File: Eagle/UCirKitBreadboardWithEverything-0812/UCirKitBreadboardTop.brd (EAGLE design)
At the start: 64.8 x 100 mm, 600 parts

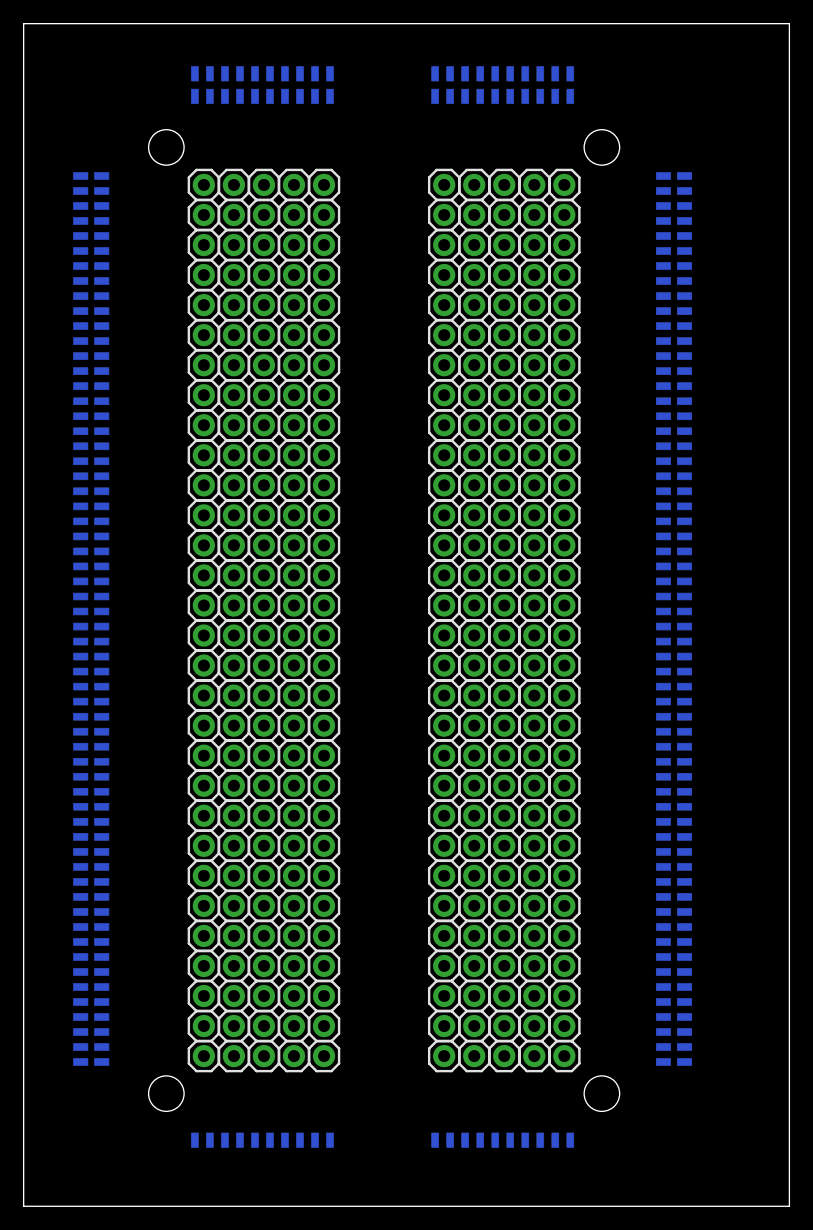
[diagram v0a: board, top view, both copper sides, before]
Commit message: UCirKitBreadboardTop completes routing!
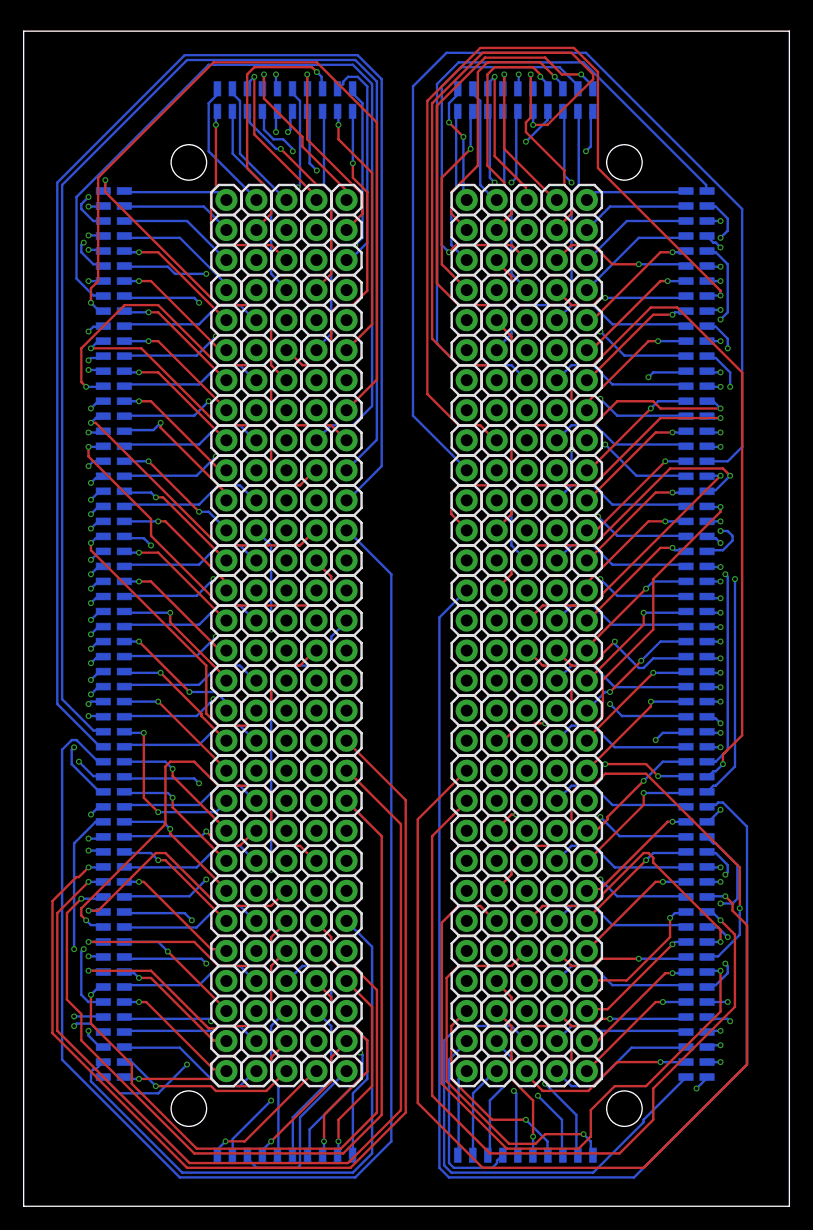
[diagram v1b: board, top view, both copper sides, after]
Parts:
- moved JP1022 2.29 mm to (56.0, 84.6)
- moved JP1026 2.29 mm to (56.0, 79.5)
- moved JP1029 2.29 mm to (56.0, 75.7)
- moved JP1033 2.29 mm to (56.0, 70.6)
- moved JP1037 2.29 mm to (56.0, 65.5)
- moved JP63 2.29 mm to (22.2, 69.8)
- moved JP64 2.29 mm to (24.8, 69.8)
- moved JP65 2.29 mm to (27.3, 69.8)
- moved JP66 2.29 mm to (37.5, 69.8)
- moved JP67 2.29 mm to (40.0, 69.8)
- moved JP68 2.29 mm to (42.5, 69.8)
- moved JP69 2.29 mm to (45.1, 69.8)
- moved JP70 2.29 mm to (47.6, 69.8)
- moved JP83 2.29 mm to (22.2, 64.8)
- moved JP84 2.29 mm to (24.8, 64.8)
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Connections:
- net 0_1439380519 renamed 0_1439385713
- net 0_1439380547 renamed 0_1439385741
- net 0_1439380570 renamed 0_1439385798
- net 0_1439380605 renamed 0_1439385823
- net 0_1439380652 renamed 0_1439385772
- net 0_1439380747 renamed 0_1439385849
- net 10_1439380519 renamed 10_1439385713
- net 10_1439380547 renamed 10_1439385741
- net 10_1439380570 renamed 10_1439385798
- net 10_1439380605 renamed 10_1439385823
- net 10_1439380652 renamed 10_1439385772
- net 10_1439380747 renamed 10_1439385849
- net 11_1439380519 renamed 11_1439385713
- net 11_1439380547 renamed 11_1439385741
- net 11_1439380570 renamed 11_1439385798
- net 11_1439380605 renamed 11_1439385823
- net 11_1439380652 renamed 11_1439385772
- net 11_1439380747 renamed 11_1439385849
- net 12_1439380519 renamed 12_1439385713
- net 12_1439380547 renamed 12_1439385741
- net 12_1439380570 renamed 12_1439385798
- net 12_1439380605 renamed 12_1439385823
- net 12_1439380652 renamed 12_1439385772
- net 12_1439380747 renamed 12_1439385849
- net 13_1439380519 renamed 13_1439385713
- net 13_1439380547 renamed 13_1439385741
- net 13_1439380570 renamed 13_1439385798
- net 13_1439380605 renamed 13_1439385823
- net 13_1439380652 renamed 13_1439385772
- net 13_1439380747 renamed 13_1439385849
- net 14_1439380519 renamed 14_1439385713
- net 14_1439380547 renamed 14_1439385741
- net 14_1439380570 renamed 14_1439385798
- net 14_1439380605 renamed 14_1439385823
- net 14_1439380652 renamed 14_1439385772
- net 14_1439380747 renamed 14_1439385849
- net 15_1439380519 renamed 15_1439385713
- net 15_1439380547 renamed 15_1439385741
- net 15_1439380570 renamed 15_1439385798
- net 15_1439380605 renamed 15_1439385823
- net 15_1439380652 renamed 15_1439385772
- net 15_1439380747 renamed 15_1439385849
- net 16_1439380519 renamed 16_1439385713
- net 16_1439380547 renamed 16_1439385741
- net 16_1439380570 renamed 16_1439385798
- net 16_1439380605 renamed 16_1439385823
- net 16_1439380652 renamed 16_1439385772
- net 16_1439380747 renamed 16_1439385849
- net 17_1439380519 renamed 17_1439385713
- net 17_1439380547 renamed 17_1439385741
- net 17_1439380570 renamed 17_1439385798
- net 17_1439380605 renamed 17_1439385823
- net 17_1439380652 renamed 17_1439385772
- net 17_1439380747 renamed 17_1439385849
- net 18_1439380519 renamed 18_1439385713
- net 18_1439380547 renamed 18_1439385741
- net 18_1439380570 renamed 18_1439385798
- net 18_1439380605 renamed 18_1439385823
- net 18_1439380652 renamed 18_1439385772
- net 18_1439380747 renamed 18_1439385849
- net 19_1439380519 renamed 19_1439385713
- net 19_1439380547 renamed 19_1439385741
- net 19_1439380570 renamed 19_1439385798
- net 19_1439380605 renamed 19_1439385823
- net 19_1439380652 renamed 19_1439385772
- net 19_1439380747 renamed 19_1439385849
- net 1_1439380519 renamed 1_1439385713
- net 1_1439380547 renamed 1_1439385741
- net 1_1439380570 renamed 1_1439385798
- net 1_1439380605 renamed 1_1439385823
- net 1_1439380652 renamed 1_1439385772
- net 1_1439380747 renamed 1_1439385849
- net 20_1439380519 renamed 20_1439385713
- net 20_1439380547 renamed 20_1439385741
- net 20_1439380570 renamed 20_1439385798
- net 20_1439380605 renamed 20_1439385823
- net 20_1439380652 renamed 20_1439385772
- net 20_1439380747 renamed 20_1439385849
- net 21_1439380519 renamed 21_1439385713
- net 21_1439380547 renamed 21_1439385741
- net 21_1439380570 renamed 21_1439385798
- net 21_1439380605 renamed 21_1439385823
- net 21_1439380652 renamed 21_1439385772
- net 21_1439380747 renamed 21_1439385849
- net 22_1439380519 renamed 22_1439385713
- net 22_1439380547 renamed 22_1439385741
- net 22_1439380570 renamed 22_1439385798
- net 22_1439380605 renamed 22_1439385823
- net 22_1439380652 renamed 22_1439385772
- net 22_1439380747 renamed 22_1439385849
- net 23_1439380519 renamed 23_1439385713
- net 23_1439380547 renamed 23_1439385741
- net 23_1439380570 renamed 23_1439385798
- net 23_1439380605 renamed 23_1439385823
- net 23_1439380652 renamed 23_1439385772
- net 23_1439380747 renamed 23_1439385849
- net 24_1439380519 renamed 24_1439385713
- net 24_1439380547 renamed 24_1439385741
- net 24_1439380570 renamed 24_1439385798
- net 24_1439380605 renamed 24_1439385823
- net 24_1439380652 renamed 24_1439385772
- net 24_1439380747 renamed 24_1439385849
- net 25_1439380519 renamed 25_1439385713
- net 25_1439380547 renamed 25_1439385741
- net 25_1439380570 renamed 25_1439385798
- net 25_1439380605 renamed 25_1439385823
- net 25_1439380652 renamed 25_1439385772
- net 25_1439380747 renamed 25_1439385849
- net 26_1439380519 renamed 26_1439385713
- net 26_1439380547 renamed 26_1439385741
- net 26_1439380570 renamed 26_1439385798
- net 26_1439380605 renamed 26_1439385823
- net 26_1439380652 renamed 26_1439385772
- net 26_1439380747 renamed 26_1439385849
- net 27_1439380519 renamed 27_1439385713
- net 27_1439380547 renamed 27_1439385741
- net 27_1439380570 renamed 27_1439385798
- net 27_1439380605 renamed 27_1439385823
- net 27_1439380652 renamed 27_1439385772
- net 27_1439380747 renamed 27_1439385849
- net 28_1439380519 renamed 28_1439385713
- net 28_1439380547 renamed 28_1439385741
- net 28_1439380570 renamed 28_1439385798
- net 28_1439380605 renamed 28_1439385823
- net 28_1439380652 renamed 28_1439385772
- net 28_1439380747 renamed 28_1439385849
- net 29_1439380519 renamed 29_1439385713
- net 29_1439380547 renamed 29_1439385741
- net 29_1439380570 renamed 29_1439385798
- net 29_1439380605 renamed 29_1439385823
- net 29_1439380652 renamed 29_1439385772
- net 29_1439380747 renamed 29_1439385849
- net 2_1439380519 renamed 2_1439385713
- net 2_1439380547 renamed 2_1439385741
- net 2_1439380570 renamed 2_1439385798
- net 2_1439380605 renamed 2_1439385823
- net 2_1439380652 renamed 2_1439385772
- net 2_1439380747 renamed 2_1439385849
- net 30_1439380519 renamed 30_1439385713
- net 30_1439380570 renamed 30_1439385798
- net 30_1439380652 renamed 30_1439385772
- net 30_1439380747 renamed 30_1439385849
- net 31_1439380519 renamed 31_1439385713
- net 31_1439380570 renamed 31_1439385798
- net 31_1439380652 renamed 31_1439385772
- net 31_1439380747 renamed 31_1439385849
- net 32_1439380519 renamed 32_1439385713
- net 32_1439380570 renamed 32_1439385798
- net 32_1439380652 renamed 32_1439385772
- net 32_1439380747 renamed 32_1439385849
- net 33_1439380519 renamed 33_1439385713
- net 33_1439380570 renamed 33_1439385798
- net 33_1439380652 renamed 33_1439385772
- net 33_1439380747 renamed 33_1439385849
- net 34_1439380519 renamed 34_1439385713
- net 34_1439380570 renamed 34_1439385798
- net 34_1439380652 renamed 34_1439385772
- net 34_1439380747 renamed 34_1439385849
- net 35_1439380519 renamed 35_1439385713
- net 35_1439380570 renamed 35_1439385798
- net 35_1439380652 renamed 35_1439385772
- net 35_1439380747 renamed 35_1439385849
- net 36_1439380519 renamed 36_1439385713
- net 36_1439380570 renamed 36_1439385798
- net 36_1439380652 renamed 36_1439385772
- net 36_1439380747 renamed 36_1439385849
- net 37_1439380519 renamed 37_1439385713
- net 37_1439380570 renamed 37_1439385798
- net 37_1439380652 renamed 37_1439385772
- net 37_1439380747 renamed 37_1439385849
- net 38_1439380519 renamed 38_1439385713
- net 38_1439380570 renamed 38_1439385798
- net 38_1439380652 renamed 38_1439385772
- net 38_1439380747 renamed 38_1439385849
- net 39_1439380519 renamed 39_1439385713
- net 39_1439380570 renamed 39_1439385798
- net 39_1439380652 renamed 39_1439385772
- net 39_1439380747 renamed 39_1439385849
- net 3_1439380519 renamed 3_1439385713
- net 3_1439380547 renamed 3_1439385741
- net 3_1439380570 renamed 3_1439385798
- net 3_1439380605 renamed 3_1439385823
- net 3_1439380652 renamed 3_1439385772
- net 3_1439380747 renamed 3_1439385849
- net 40_1439380519 renamed 40_1439385713
- net 40_1439380570 renamed 40_1439385798
- net 40_1439380652 renamed 40_1439385772
- net 40_1439380747 renamed 40_1439385849
- net 41_1439380519 renamed 41_1439385713
- net 41_1439380570 renamed 41_1439385798
- net 41_1439380652 renamed 41_1439385772
- net 41_1439380747 renamed 41_1439385849
- net 42_1439380519 renamed 42_1439385713
- net 42_1439380570 renamed 42_1439385798
- net 42_1439380652 renamed 42_1439385772
- net 42_1439380747 renamed 42_1439385849
- net 43_1439380519 renamed 43_1439385713
- net 43_1439380570 renamed 43_1439385798
- net 43_1439380652 renamed 43_1439385772
- net 43_1439380747 renamed 43_1439385849
- net 44_1439380519 renamed 44_1439385713
- net 44_1439380570 renamed 44_1439385798
- net 44_1439380652 renamed 44_1439385772
- net 44_1439380747 renamed 44_1439385849
- net 45_1439380519 renamed 45_1439385713
- net 45_1439380570 renamed 45_1439385798
- net 45_1439380652 renamed 45_1439385772
- net 45_1439380747 renamed 45_1439385849
- net 46_1439380519 renamed 46_1439385713
- net 46_1439380570 renamed 46_1439385798
- net 46_1439380652 renamed 46_1439385772
- net 46_1439380747 renamed 46_1439385849
- net 47_1439380519 renamed 47_1439385713
- net 47_1439380570 renamed 47_1439385798
- net 47_1439380652 renamed 47_1439385772
- net 47_1439380747 renamed 47_1439385849
- net 48_1439380519 renamed 48_1439385713
- net 48_1439380570 renamed 48_1439385798
- net 48_1439380652 renamed 48_1439385772
- net 48_1439380747 renamed 48_1439385849
- net 49_1439380519 renamed 49_1439385713
- net 49_1439380570 renamed 49_1439385798
- net 49_1439380652 renamed 49_1439385772
- net 49_1439380747 renamed 49_1439385849
- net 4_1439380519 renamed 4_1439385713
- net 4_1439380547 renamed 4_1439385741
- net 4_1439380570 renamed 4_1439385798
- net 4_1439380605 renamed 4_1439385823
- net 4_1439380652 renamed 4_1439385772
- net 4_1439380747 renamed 4_1439385849
- net 50_1439380519 renamed 50_1439385713
- net 50_1439380570 renamed 50_1439385798
- net 50_1439380652 renamed 50_1439385772
- net 50_1439380747 renamed 50_1439385849
- net 51_1439380519 renamed 51_1439385713
- net 51_1439380570 renamed 51_1439385798
- net 51_1439380652 renamed 51_1439385772
- net 51_1439380747 renamed 51_1439385849
- net 52_1439380519 renamed 52_1439385713
- net 52_1439380570 renamed 52_1439385798
- net 52_1439380652 renamed 52_1439385772
- net 52_1439380747 renamed 52_1439385849
- net 53_1439380519 renamed 53_1439385713
- net 53_1439380570 renamed 53_1439385798
- net 53_1439380652 renamed 53_1439385772
- net 53_1439380747 renamed 53_1439385849
- net 54_1439380519 renamed 54_1439385713
- net 54_1439380570 renamed 54_1439385798
- net 54_1439380652 renamed 54_1439385772
- net 54_1439380747 renamed 54_1439385849
- net 55_1439380519 renamed 55_1439385713
- net 55_1439380570 renamed 55_1439385798
- net 55_1439380652 renamed 55_1439385772
- net 55_1439380747 renamed 55_1439385849
- net 56_1439380519 renamed 56_1439385713
- net 56_1439380570 renamed 56_1439385798
- net 56_1439380652 renamed 56_1439385772
- net 56_1439380747 renamed 56_1439385849
- net 57_1439380519 renamed 57_1439385713
- net 57_1439380570 renamed 57_1439385798
- net 57_1439380652 renamed 57_1439385772
- net 57_1439380747 renamed 57_1439385849
- net 58_1439380519 renamed 58_1439385713
- net 58_1439380570 renamed 58_1439385798
- net 58_1439380652 renamed 58_1439385772
- net 58_1439380747 renamed 58_1439385849
- net 59_1439380519 renamed 59_1439385713
- net 59_1439380570 renamed 59_1439385798
- net 59_1439380652 renamed 59_1439385772
- net 59_1439380747 renamed 59_1439385849
- net 5_1439380519 renamed 5_1439385713
- net 5_1439380547 renamed 5_1439385741
- net 5_1439380570 renamed 5_1439385798
- net 5_1439380605 renamed 5_1439385823
- net 5_1439380652 renamed 5_1439385772
- net 5_1439380747 renamed 5_1439385849
- net 6_1439380519 renamed 6_1439385713
- net 6_1439380547 renamed 6_1439385741
- net 6_1439380570 renamed 6_1439385798
- net 6_1439380605 renamed 6_1439385823
- net 6_1439380652 renamed 6_1439385772
- net 6_1439380747 renamed 6_1439385849
- net 7_1439380519 renamed 7_1439385713
- net 7_1439380547 renamed 7_1439385741
- net 7_1439380570 renamed 7_1439385798
- net 7_1439380605 renamed 7_1439385823
- net 7_1439380652 renamed 7_1439385772
- net 7_1439380747 renamed 7_1439385849
- net 8_1439380519 renamed 8_1439385713
- net 8_1439380547 renamed 8_1439385741
- net 8_1439380570 renamed 8_1439385798
- net 8_1439380605 renamed 8_1439385823
- net 8_1439380652 renamed 8_1439385772
- net 8_1439380747 renamed 8_1439385849
- net 9_1439380519 renamed 9_1439385713
- net 9_1439380547 renamed 9_1439385741
- net 9_1439380570 renamed 9_1439385798
- net 9_1439380605 renamed 9_1439385823
- net 9_1439380652 renamed 9_1439385772
- net 9_1439380747 renamed 9_1439385849
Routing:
- net 58_1439385772: track 0.00 -> 119.2 mm
- net 57_1439385772: track 0.00 -> 117.3 mm
- net 59_1439385772: track 0.00 -> 113.8 mm
- net 56_1439385849: track 0.00 -> 104.6 mm
- net 18_1439385849: track 0.00 -> 92.4 mm
- net 50_1439385772: track 0.00 -> 86.7 mm, vias 0 -> 1
- net 49_1439385772: track 0.00 -> 81.1 mm, vias 0 -> 1
- net 50_1439385849: track 0.00 -> 80.1 mm, vias 0 -> 1
- net 58_1439385849: track 0.00 -> 77.2 mm, vias 0 -> 1
- net 7_1439385849: track 0.00 -> 73.7 mm, vias 0 -> 1
- net 48_1439385772: track 0.00 -> 73.5 mm, vias 0 -> 1
- net 7_1439385772: track 0.00 -> 73.2 mm
- net 49_1439385849: track 0.00 -> 69.7 mm, vias 0 -> 1
- net 8_1439385772: track 0.00 -> 67.3 mm, vias 0 -> 1
- net 53_1439385772: track 0.00 -> 60.0 mm, vias 0 -> 1
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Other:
- board size 64.8 x 100 mm -> 64.8 x 99.4 mm
